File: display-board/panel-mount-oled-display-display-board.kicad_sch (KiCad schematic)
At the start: 2 parts, among them J1 Conn_01x08_Pin, J2 Conn_01x08_Pin

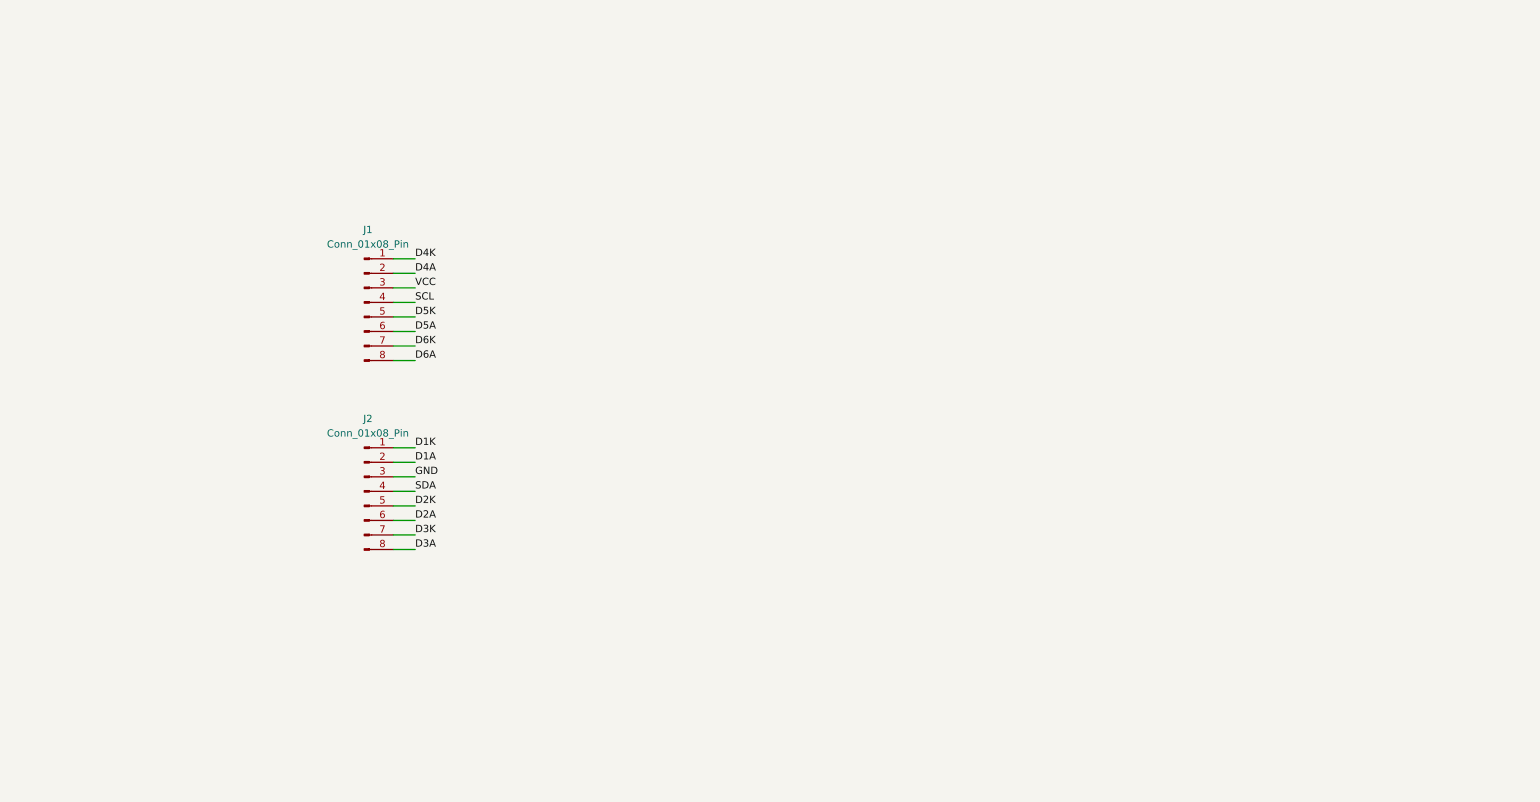
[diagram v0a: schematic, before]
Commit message: display: OLED handsolder footprint, schematic/PCB update, datasheets and backups
- Assign Display_Handsoldering OLED-128O064D_Handsoldering footprint and refresh board

- Update fp-lib-table and fp-info-cache

- Add datasheet PDFs, project backup zips, remove superseded connector backup
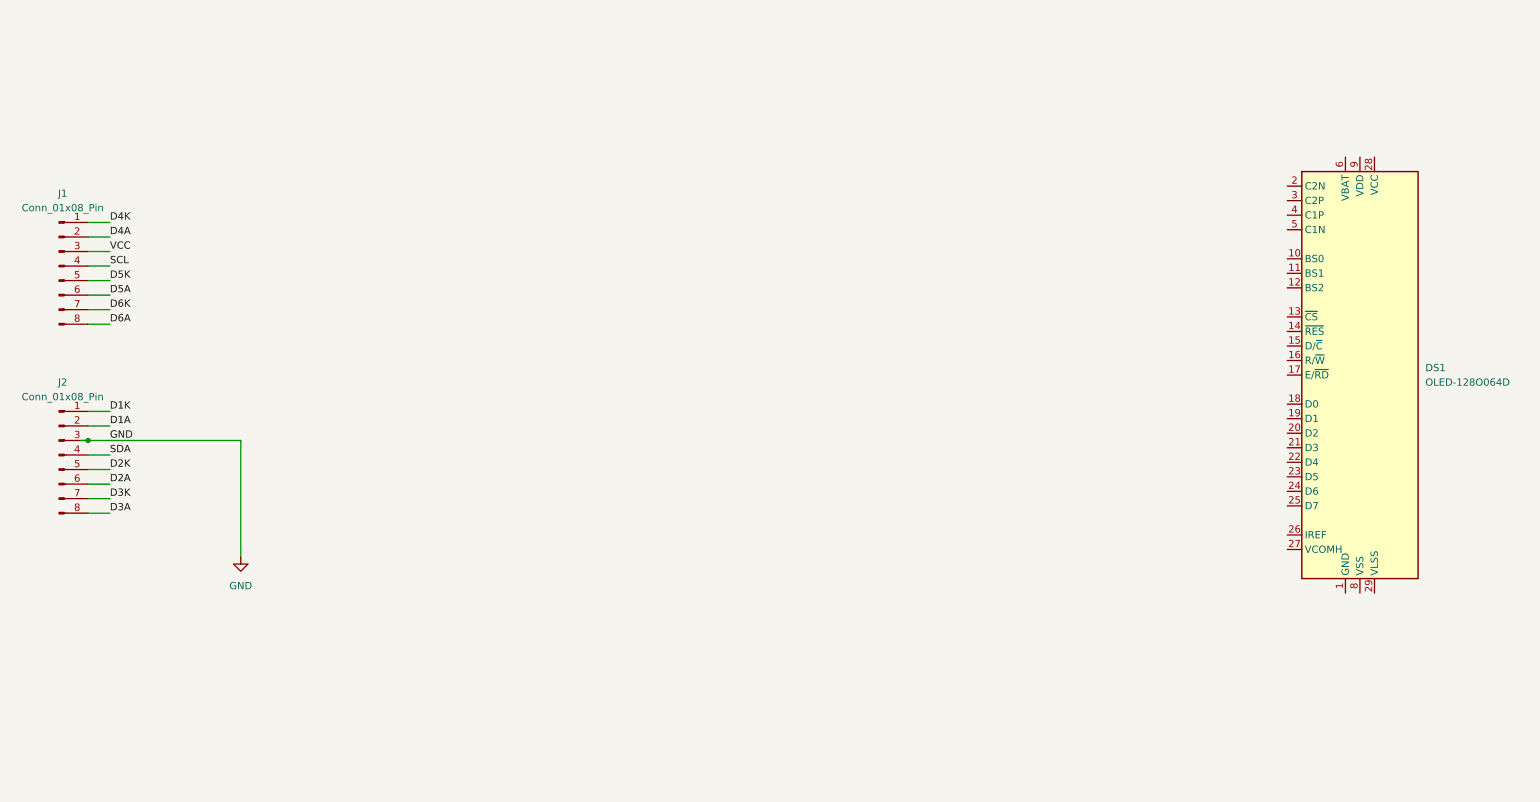
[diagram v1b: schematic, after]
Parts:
- added DS1: OLED-128O064D, Display_Handsoldering:OLED-128O064D_Handsoldering, symbol Display_Graphic:OLED-128O064D
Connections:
- new net: DS1.1 (GND), DS1.30 (GND)
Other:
- moved on the sheet: J1, J2

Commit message: Expand display board schematic with additional components
Update KiCad schematic and PCB to reflect new circuitry. Refresh
project backup archives and remove superseded backup snapshot.
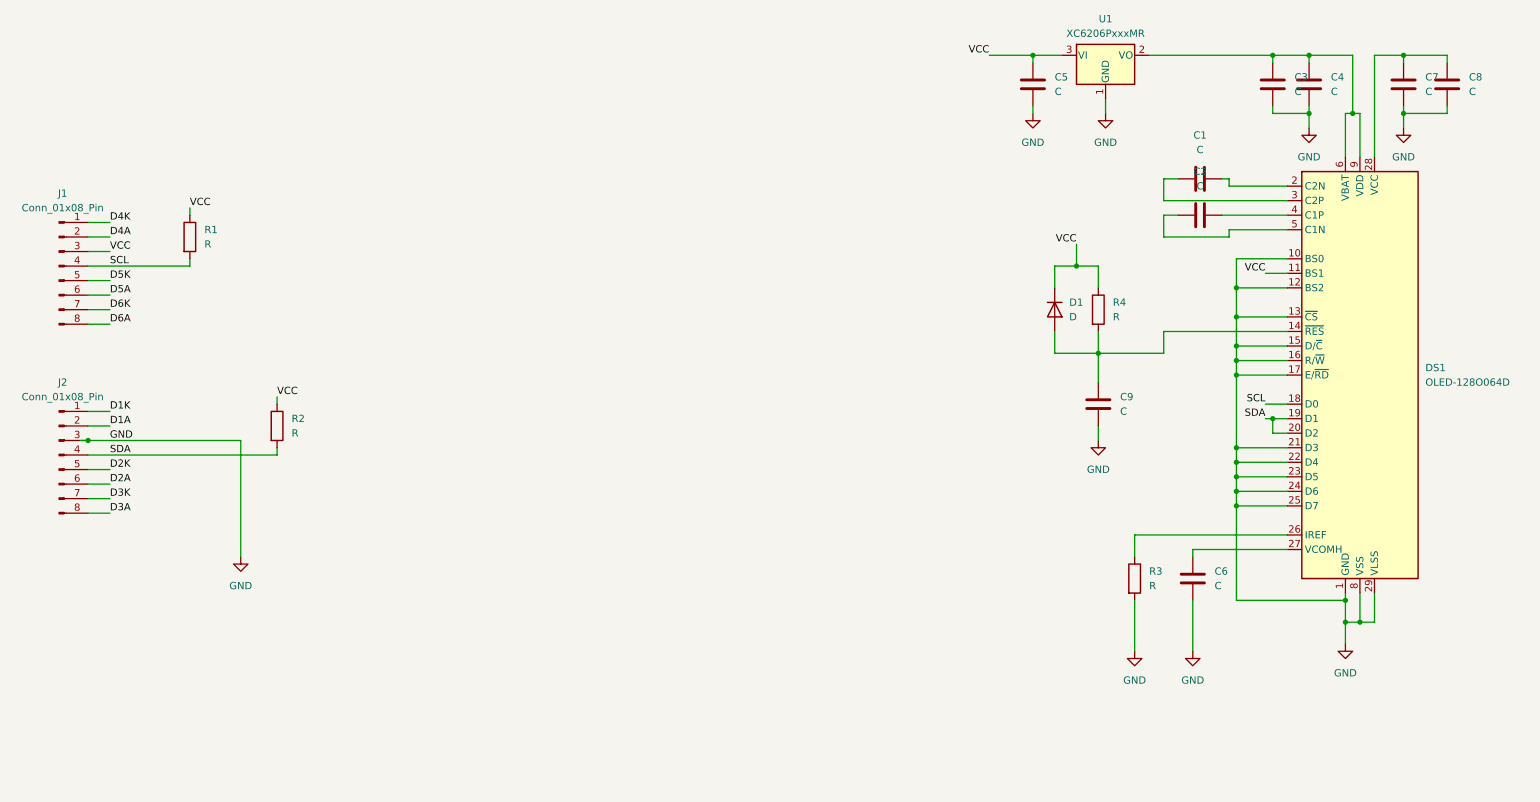
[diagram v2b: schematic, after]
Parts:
- added C1, C2, C3, C4, C5, C6, C7, C8, C9: C, Capacitor_SMD:C_0805_2012Metric_Pad1.18x1.45mm_HandSolder, symbol Device:C
- added D1: D, Diode_SMD:D_MiniMELF_Handsoldering, symbol Device:D
- added R1, R2, R3, R4: R, Resistor_SMD:R_0805_2012Metric_Pad1.20x1.40mm_HandSolder, symbol Device:R
- added U1: XC6206PxxxMR, Package_TO_SOT_SMD:SOT-23-3, symbol Regulator_Linear:XC6206PxxxMR
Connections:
- net GND: now also DS1.1 (GND), DS1.10 (BS0), DS1.12 (BS2), DS1.13 (~{CS}), DS1.15 (D/~{C}), DS1.16 (R/~{W}), DS1.17 (E/~{RD}), DS1.21 (D3), DS1.22 (D4), DS1.23 (D5), DS1.24 (D6), DS1.25 (D7), DS1.29 (VLSS), DS1.30 (GND), DS1.8 (VSS), C3.1, C4.1, C5.1, C6.1, C7.1, C8.1, C9.1, R3.2, U1.1 (GND)
- net SCL: now also DS1.18 (D0), R1.2
- net SDA: now also DS1.19 (D1), DS1.20 (D2), R2.2
- net VCC: now also DS1.11 (BS1), C5.2, D1.1 (K), R1.1, R2.1, R4.1, U1.3 (VI)
- net at DS1.14 (~{RES}): now also C9.2, D1.2 (A), R4.2
- net at DS1.2 (C2N): now also C1.1
- net at DS1.26 (IREF): now also R3.1
- net at DS1.27 (VCOMH): now also C6.2
- net at DS1.28 (VCC): now also C7.2, C8.2
- net at DS1.3 (C2P): now also C1.2
- net at DS1.4 (C1P): now also C2.1
- net at DS1.5 (C1N): now also C2.2
- net at DS1.6 (VBAT): now also DS1.9 (VDD), C3.2, C4.2, U1.2 (VO)

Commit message: display: finish board routing and checkpoint KiCad outputs
Capture the fully routed display board together with the generated KiCad
artifacts and fresh backups for this layout milestone.
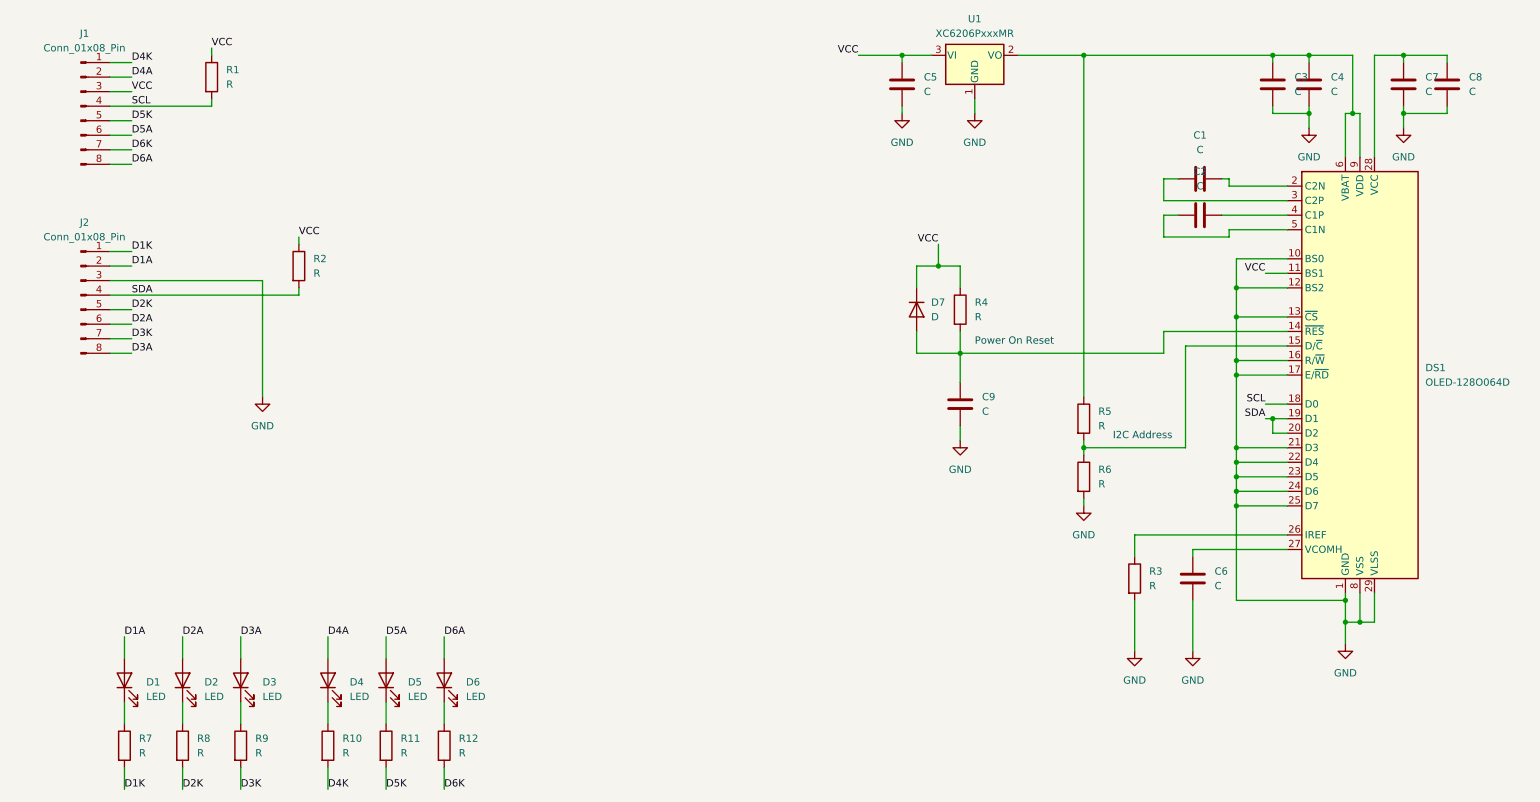
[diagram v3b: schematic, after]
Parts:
- added D1, D2, D3, D4, D5, D6: LED, LED_SMD:LED_0805_2012Metric_Pad1.15x1.40mm_HandSolder, symbol Device:LED
- added R10, R11, R12, R5, R6, R7, R8, R9: R, Resistor_SMD:R_0805_2012Metric_Pad1.20x1.40mm_HandSolder, symbol Device:R
- renumbered D1 to D7
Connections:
- net D1A: now also D1.2 (A)
- net D1K: now also R7.2
- net D2A: now also D2.2 (A)
- net D2K: now also R8.2
- net D3A: now also D3.2 (A)
- net D3K: now also R9.2
- net D4A: now also D4.2 (A)
- net D4K: now also R10.2
- net D5A: now also D5.2 (A)
- net D5K: now also R11.2
- net D6A: now also D6.2 (A)
- net D6K: now also R12.2
- net GND: now also R6.2; no longer DS1.15 (D/~{C})
- net at C3.2, C4.2, DS1.6 (VBAT)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: now also R5.1
- new net: DS1.15 (D/~{C}), R5.2, R6.1
- new net: D5.1 (K), R11.1
- new net: D4.1 (K), R10.1
- new net: D1.1 (K), R7.1
- new net: D6.1 (K), R12.1
- new net: D3.1 (K), R9.1
- new net: D2.1 (K), R8.1
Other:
- note added: "I2C Address"
- note added: "Power On Reset"
- moved on the sheet: C5, C9, D7, J1, J2, R1, R2, R4, U1
